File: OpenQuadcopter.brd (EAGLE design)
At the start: 76 x 76 mm, 78 parts, among them U1 MPU-6050QFN-24

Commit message: update PB6
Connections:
- net SDL/PB6 renamed SCL/PB6
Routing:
- net SCL/PB6: track 14.7 -> 13.6 mm
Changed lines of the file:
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@@
 <wire x1="-9.406" y1="-1.524" x2="-9.5" y2="-1.43" width="0.254" layer="1"/>
-</signal>
-<signal name="SDL/PB6">
-<contactref element="U$11" pad="7"/>
-<contactref element="U1" pad="23"/>
-<wire x1="-10.668" y1="-0.508" x2="-6.604" y2="-0.508" width="0.254" layer="1"/>
-<wire x1="-6.604" y1="-0.508" x2="-3.048" y2="3.048" width="0.254" layer="1"/>
-<wire x1="-3.048" y1="3.048" x2="-3.048" y2="3.81" width="0.254" layer="1"/>
-<wire x1="-3.048" y1="3.81" x2="-2.54" y2="4.318" width="0.254" layer="1"/>
-<wire x1="-2.54" y1="4.318" x2="-2.0817" y2="4.318" width="0.254" layer="1"/>
-<wire x1="-2.0817" y1="4.318" x2="-2.0816" y2="4.3179" width="0.254" layer="1"/>
-<wire x1="-12.5" y1="-3.43" x2="-12.5" y2="-2.34" width="0.254" layer="1"/>
-<wire x1="-12.5" y1="-2.34" x2="-10.668" y2="-0.508" width="0.254" layer="1"/>
 </signal>
 <signal name="INT/PA4">
@@
 <wire x1="-1.016" y1="1.27" x2="-3.556" y2="1.27" width="0.254" layer="16"/>
 </signal>
+<signal name="SCL/PB6">
+<contactref element="U$11" pad="7"/>
+<contactref element="U1" pad="23"/>
+<wire x1="-10.668" y1="-0.508" x2="-6.604" y2="-0.508" width="0.254" layer="1"/>
+<wire x1="-6.604" y1="-0.508" x2="-3.048" y2="3.048" width="0.254" layer="1"/>
+<wire x1="-3.048" y1="3.048" x2="-3.048" y2="3.81" width="0.254" layer="1"/>
+<wire x1="-3.048" y1="3.81" x2="-2.54" y2="4.318" width="0.254" layer="1"/>
+<wire x1="-2.54" y1="4.318" x2="-2.0817" y2="4.318" width="0.254" layer="1"/>
+<wire x1="-2.0817" y1="4.318" x2="-2.0816" y2="4.3179" width="0.254" layer="1"/>
+<wire x1="-12.5" y1="-2.34" x2="-10.668" y2="-0.508" width="0.254" layer="1"/>
+<wire x1="-12.5" y1="-2.34" x2="-12.5" y2="-3.43" width="0" layer="19" extent="1-1"/>
+</signal>
 </signals>

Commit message: Correct the name PMV31XN.
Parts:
- U$2, U$4, U$6, U$8: value PWV31XN -> PMV31XN
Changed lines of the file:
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@@
 <attribute name="VALUE" x="-2.667" y="-6.858" size="0.6096" layer="27"/>
 </element>
-<element name="U$2" library="openmotestm" package="SOT23-W" value="PWV31XN" x="-2.921" y="25.273" smashed="yes">
+<element name="U$2" library="openmotestm" package="SOT23-W" value="PMV31XN" x="-2.921" y="25.273" smashed="yes">
 <attribute name="NAME" x="-3.809" y="27.727" size="0.6096" layer="25"/>
 <attribute name="VALUE" x="-5.167" y="23.073" size="0.6096" layer="27" rot="R90"/>
@@
 <attribute name="VALUE" x="-2.286" y="23.622" size="0.6096" layer="27" rot="R180"/>
 </element>
-<element name="U$4" library="openmotestm" package="SOT23-W" value="PWV31XN" x="-25.019" y="-2.159" smashed="yes" rot="R90">
+<element name="U$4" library="openmotestm" package="SOT23-W" value="PMV31XN" x="-25.019" y="-2.159" smashed="yes" rot="R90">
 <attribute name="NAME" x="-27.473" y="-3.047" size="0.6096" layer="25" rot="R90"/>
 <attribute name="VALUE" x="-22.819" y="-4.405" size="0.6096" layer="27" rot="R180"/>
@@
 <attribute name="VALUE" x="-23.241" y="-1.524" size="0.6096" layer="27" rot="R270"/>
 </element>
-<element name="U$6" library="openmotestm" package="SOT23-W" value="PWV31XN" x="1.905" y="-25.273" smashed="yes" rot="R180">
+<element name="U$6" library="openmotestm" package="SOT23-W" value="PMV31XN" x="1.905" y="-25.273" smashed="yes" rot="R180">
 <attribute name="NAME" x="4.105" y="-24.639" size="0.6096" layer="25" rot="R270"/>
 <attribute name="VALUE" x="3.597" y="-27.773" size="0.6096" layer="27" rot="R180"/>
@@
 <attribute name="VALUE" x="1.524" y="-23.495" size="0.6096" layer="27"/>
 </element>
-<element name="U$8" library="openmotestm" package="SOT23-W" value="PWV31XN" x="24.892" y="2.286" smashed="yes" rot="R270">
+<element name="U$8" library="openmotestm" package="SOT23-W" value="PMV31XN" x="24.892" y="2.286" smashed="yes" rot="R270">
 <attribute name="NAME" x="27.346" y="2.92" size="0.6096" layer="25" rot="R270"/>
 <attribute name="VALUE" x="22.946" y="4.532" size="0.6096" layer="27"/>

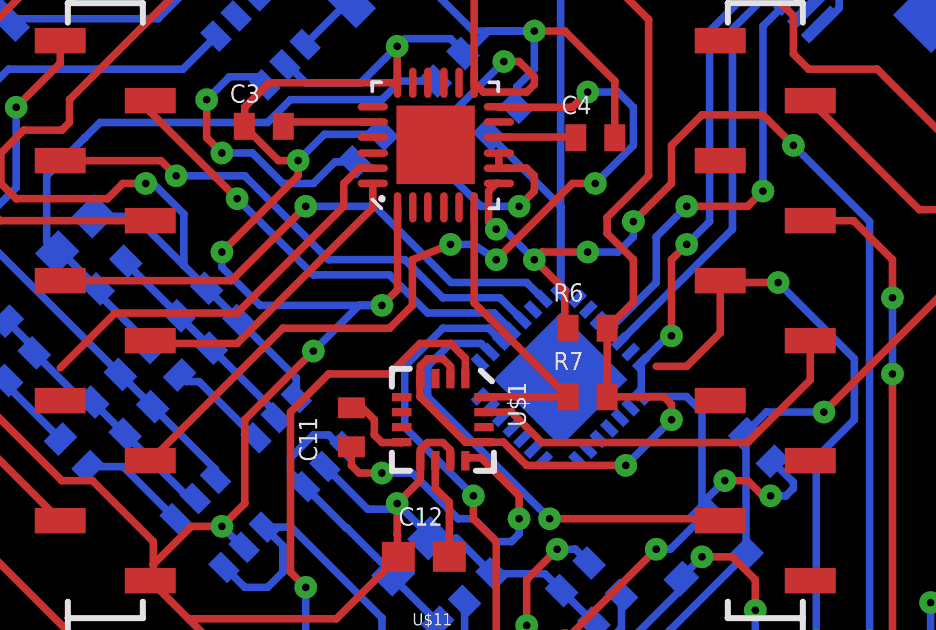
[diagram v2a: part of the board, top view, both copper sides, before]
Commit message: add 0.1uF capacitor between VDD and GND pin of CP2102.
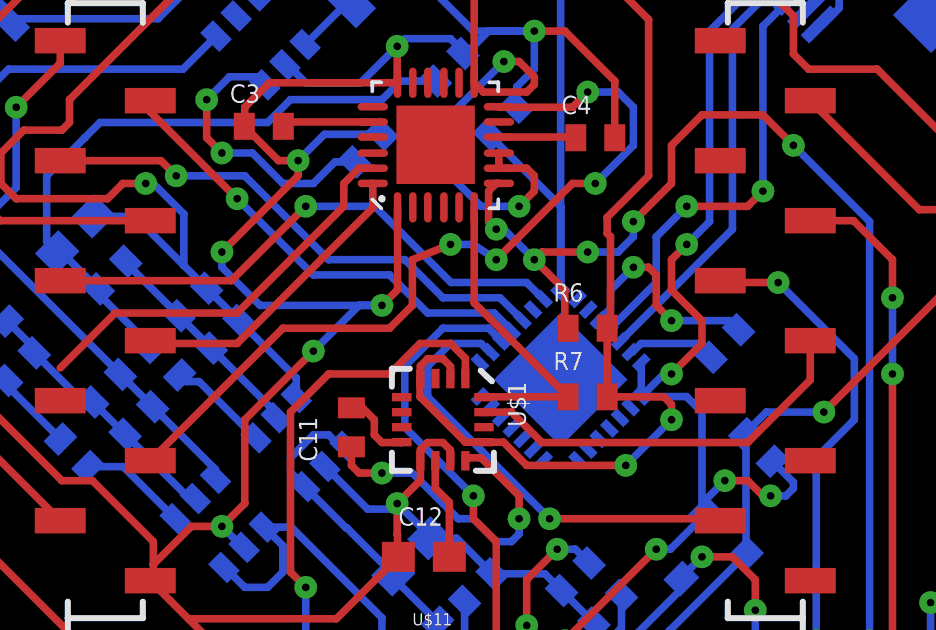
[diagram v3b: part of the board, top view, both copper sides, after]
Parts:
- added C1: 4.7uF, openmotestm:C0402
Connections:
- new net N$10: C1.2, U$14.P$3
- new net N$17: C1.1, U$14.P$6
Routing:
- net N$10: track 0.00 -> 7.20 mm, vias 0 -> 2
- net BOOT0: track 45.5 -> 41.2 mm
- net N$17: track 0.00 -> 2.99 mm
- net VBUS: track 49.4 -> 51.4 mm
- net VCCA: track 97.1 -> 96.5 mm
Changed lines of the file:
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@@
 <?xml version="1.0" encoding="utf-8"?>
 <!DOCTYPE eagle SYSTEM "eagle.dtd">
-<eagle version="6.6.0">
+<eagle version="7.5.0">
 <drawing>
 <settings>
@@
 <layer number="21" name="tPlace" color="7" fill="1" visible="yes" active="yes"/>
 <layer number="22" name="bPlace" color="7" fill="1" visible="yes" active="yes"/>
-<layer number="23" name="tOrigins" color="15" fill="1" visible="no" active="yes"/>
-<layer number="24" name="bOrigins" color="15" fill="1" visible="no" active="yes"/>
+<layer number="23" name="tOrigins" color="15" fill="1" visible="yes" active="yes"/>
+<layer number="24" name="bOrigins" color="15" fill="1" visible="yes" active="yes"/>
 <layer number="25" name="tNames" color="7" fill="1" visible="yes" active="yes"/>
 <layer number="26" name="bNames" color="7" fill="1" visible="yes" active="yes"/>
@@
 <pass name="Default">
 <param name="RoutingGrid" value="50mil"/>
+<param name="AutoGrid" value="1"/>
+<param name="Efforts" value="0"/>
+<param name="TopRouterVariant" value="1"/>
 <param name="tpViaShape" value="round"/>
 <param name="PrefDir.1" value="|"/>
@@
 <attribute name="NAME" x="-17.94374375" y="3.365821875" size="0.6096" layer="26" rot="MR315"/>
 <attribute name="VALUE" x="-16.14769375" y="1.56976875" size="0.6096" layer="28" rot="MR315"/>
+</element>
+<element name="C1" library="openmotestm" package="C0402" value="4.7uF" x="9.652" y="-1.524" smashed="yes" rot="MR135">
+<attribute name="NAME" x="10.414" y="-0.644025" size="0.6096" layer="26" rot="MR135"/>
+<attribute name="VALUE" x="7.85595" y="-0.625971875" size="1.27" layer="28" rot="MR135"/>
 </element>
 </elements>
@@
 <via x="8.382" y="1.778" extent="1-16" drill="0.254" diameter="0.254"/>
 <wire x1="8.382" y1="1.778" x2="7.874" y2="1.27" width="0.254" layer="1"/>
-<wire x1="7.874" y1="1.27" x2="7.874" y2="-1.27" width="0.254" layer="1"/>
-<via x="7.874" y="-1.27" extent="1-16" drill="0.254" diameter="0.254"/>
-<wire x1="7.874" y1="-1.27" x2="7.75728125" y2="-1.27" width="0.254" layer="16"/>
-<wire x1="7.75728125" y1="-1.27" x2="6.865884375" y2="-2.161396875" width="0.254" layer="16"/>
 <wire x1="9.207084375" y1="16.899478125" x2="8.4581125" y2="16.899478125" width="0.254" layer="16"/>
 <wire x1="8.4581125" y1="16.899478125" x2="7.19965" y2="15.641015625" width="0.254" layer="16"/>
@@
 <wire x1="11.938" y1="-6.35" x2="11.938" y2="-6.1514375" width="0.254" layer="16"/>
 <wire x1="11.938" y1="-6.1514375" x2="11.235928125" y2="-5.449365625" width="0.254" layer="16"/>
+<wire x1="7.874" y1="1.27" x2="7.874" y2="0.254" width="0.254" layer="1"/>
+<wire x1="7.874" y1="0.254" x2="8.89" y2="-0.762" width="0.254" layer="1"/>
+<wire x1="8.89" y1="-0.762" x2="8.89" y2="-1.524" width="0.254" layer="1"/>
+<wire x1="8.89" y1="-1.524" x2="7.874" y2="-2.54" width="0.254" layer="1"/>
+<via x="7.874" y="-2.54" extent="1-16" drill="0.254" diameter="0.254"/>
+<wire x1="7.874" y1="-2.54" x2="7.618653125" y2="-2.54" width="0.254" layer="16"/>
+<wire x1="7.618653125" y1="-2.54" x2="6.865884375" y2="-3.29276875" width="0.254" layer="16"/>
 </signal>
 <signal name="N$15">
@@
 <wire x1="-9.398" y1="3.81" x2="-8.382" y2="2.794" width="0.254" layer="16"/>
 <wire x1="-8.382" y1="2.794" x2="-8.382" y2="1.078603125" width="0.254" layer="16"/>
-<wire x1="-8.382" y1="1.078603125" x2="-8.350696875" y2="1.0473" width="0.254" layer="16"/>
-<wire x1="-8.350696875" y1="1.0473" x2="-7.622609375" y2="0.3192125" width="0.254" layer="16"/>
+<wire x1="-8.382" y1="1.078603125" x2="-7.622609375" y2="0.3192125" width="0.254" layer="16"/>
 <wire x1="-4.55394375" y1="13.32" x2="-2.013946875" y2="13.32" width="0.254" layer="1"/>
 <wire x1="2.794" y1="4.318" x2="3.048" y2="4.318" width="0.254" layer="1"/>
@@
 <wire x1="3.302" y1="3.556" x2="2.794" y2="3.048" width="0.254" layer="1"/>
 <wire x1="5.73" y1="2.682" x2="5.73" y2="2.144" width="0.254" layer="1"/>
-<wire x1="5.73" y1="2.144" x2="6.604" y2="1.27" width="0.254" layer="1"/>
-<wire x1="6.604" y1="1.27" x2="6.604" y2="-0.142" width="0.254" layer="1"/>
-<wire x1="6.604" y1="-0.142" x2="5.73" y2="-1.016" width="0.254" layer="1"/>
+<wire x1="5.842" y1="-0.904" x2="5.73" y2="-1.016" width="0.254" layer="1"/>
 <contactref element="C16" pad="1"/>
 <wire x1="-11.400778125" y1="2.714915625" x2="-10.0183125" y2="2.714915625" width="0.254" layer="16"/>
 <wire x1="-10.0183125" y1="2.714915625" x2="-8.382" y2="1.078603125" width="0.254" layer="16"/>
+<wire x1="5.842" y1="-0.904" x2="5.842" y2="2.032" width="0.254" layer="1"/>
+<wire x1="5.842" y1="2.032" x2="5.73" y2="2.144" width="0.254" layer="1"/>
 </signal>
 <signal name="BATTERY_IN">
@@
 <contactref element="U$11" pad="16"/>
 <contactref element="U$14" pad="P$24"/>
-<wire x1="9.5" y1="0.57" x2="9.5" y2="-1.168" width="0.254" layer="1"/>
-<wire x1="9.5" y1="-1.168" x2="8.382" y2="-2.286" width="0.254" layer="1"/>
-<wire x1="8.382" y1="-2.286" x2="7.366" y2="-2.286" width="0.254" layer="1"/>
 <wire x1="2.19898125" y1="-1.454290625" x2="2.19898125" y2="-1.43698125" width="0.254" layer="16"/>
 <wire x1="2.19898125" y1="-1.43698125" x2="1.778" y2="-1.016" width="0.254" layer="16"/>
@@
 <wire x1="-12.5" y1="-2.34" x2="-12.5" y2="-3.43" width="0" layer="19" extent="1-1"/>
 </signal>
+<signal name="N$10">
+<contactref element="U$14" pad="P$3"/>
+<contactref element="C1" pad="2"/>
+<wire x1="5.451671875" y1="-0.747184375" x2="5.842" y2="-0.35685625" width="0.254" layer="16"/>
+<wire x1="5.842" y1="-0.35685625" x2="5.842" y2="0.254" width="0.254" layer="16"/>
+<wire x1="5.842" y1="0.254" x2="6.604" y2="1.016" width="0.254" layer="16"/>
+<via x="6.604" y="1.016" extent="1-16" drill="0.254" diameter="0.254"/>
+<wire x1="6.604" y1="1.016" x2="7.112" y2="1.016" width="0.254" layer="1"/>
+<wire x1="7.112" y1="1.016" x2="7.366" y2="0.762" width="0.254" layer="1"/>
+<wire x1="7.366" y1="0.762" x2="7.366" y2="-0.254" width="0.254" layer="1"/>
+<wire x1="7.366" y1="-0.254" x2="7.874" y2="-0.762" width="0.254" layer="1"/>
+<via x="7.874" y="-0.762" extent="1-16" drill="0.254" diameter="0.254"/>
+<wire x1="7.874" y1="-0.762" x2="9.80924375" y2="-0.762" width="0.254" layer="16"/>
+<wire x1="9.80924375" y1="-0.762" x2="10.111621875" y2="-1.064378125" width="0.254" layer="16"/>
+</signal>
+<signal name="N$17">
+<contactref element="U$14" pad="P$6"/>
+<contactref element="C1" pad="1"/>
+<wire x1="6.51233125" y1="-1.80784375" x2="6.57415625" y2="-1.80784375" width="0.254" layer="16"/>
+<wire x1="6.57415625" y1="-1.80784375" x2="6.858" y2="-1.524" width="0.254" layer="16"/>
+<wire x1="6.858" y1="-1.524" x2="8.7327625" y2="-1.524" width="0.254" layer="16"/>
+<wire x1="8.7327625" y1="-1.524" x2="9.19238125" y2="-1.98361875" width="0.254" layer="16"/>
+</signal>
 </signals>

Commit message: fixed.
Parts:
- C1: value 4.7uF -> 0.1uF
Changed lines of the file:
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@@
 <attribute name="VALUE" x="-16.14769375" y="1.56976875" size="0.6096" layer="28" rot="MR315"/>
 </element>
-<element name="C1" library="openmotestm" package="C0402" value="4.7uF" x="9.652" y="-1.524" smashed="yes" rot="MR135">
+<element name="C1" library="openmotestm" package="C0402" value="0.1uF" x="9.652" y="-1.524" smashed="yes" rot="MR135">
 <attribute name="NAME" x="10.414" y="-0.644025" size="0.6096" layer="26" rot="MR135"/>
 <attribute name="VALUE" x="7.85595" y="-0.625971875" size="1.27" layer="28" rot="MR135"/>
